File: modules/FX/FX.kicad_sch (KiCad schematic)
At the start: 0 parts

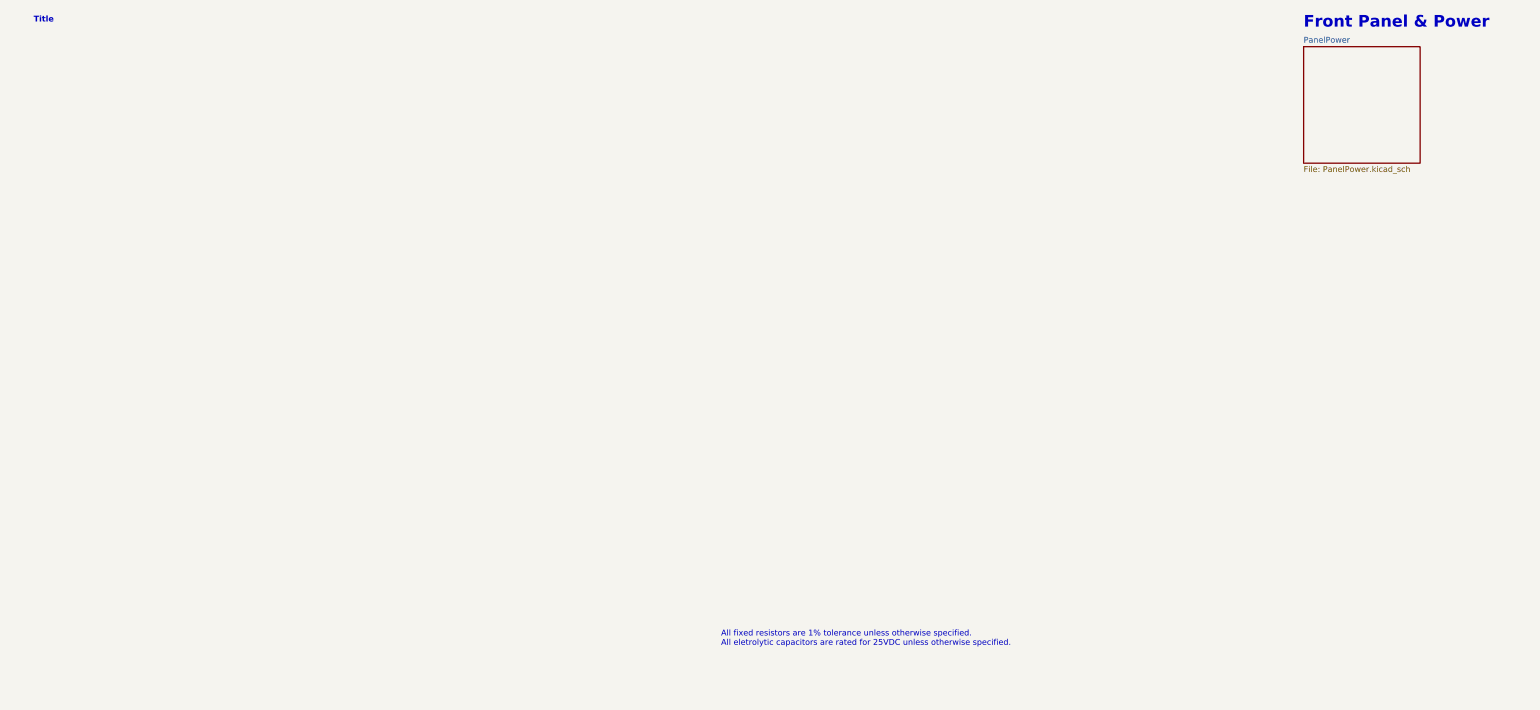
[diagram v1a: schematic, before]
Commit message: FX module - preliminary schematic done
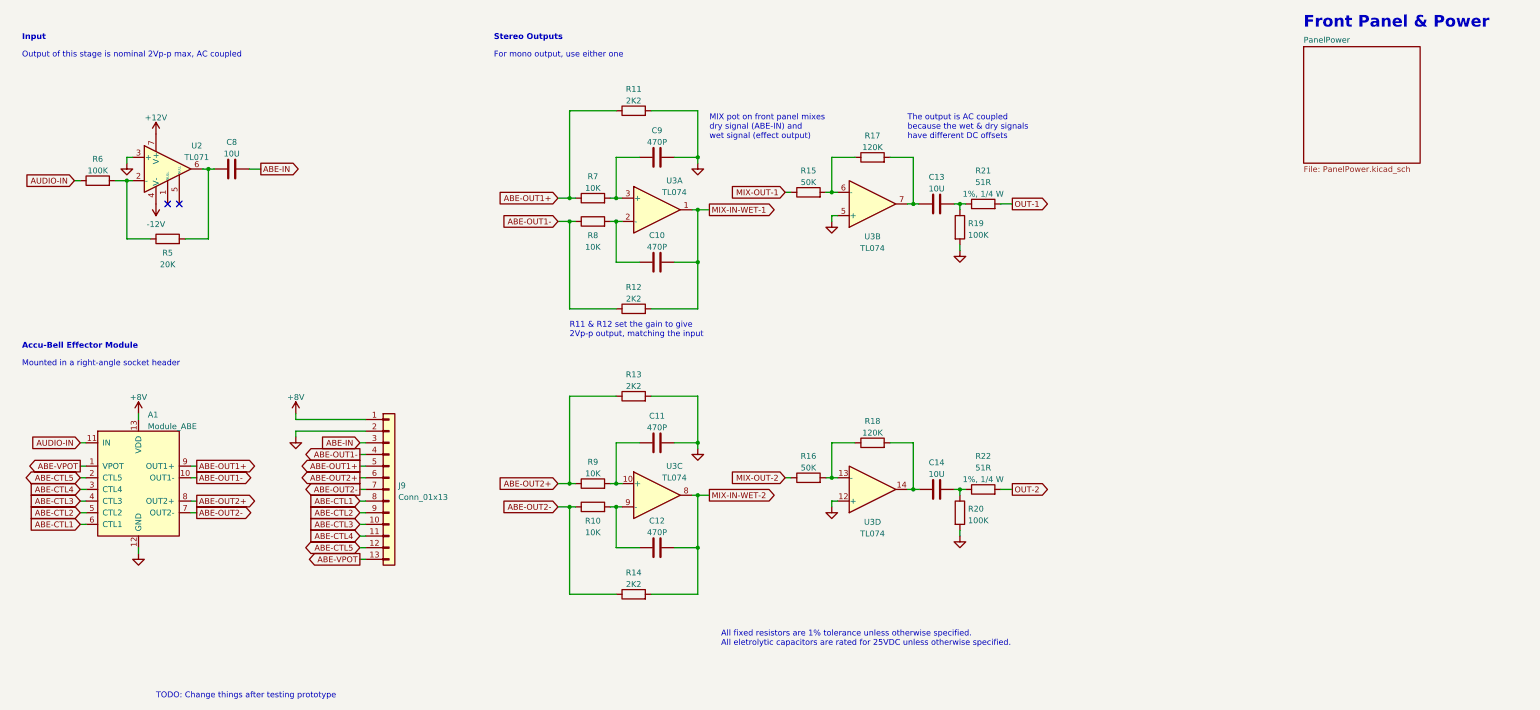
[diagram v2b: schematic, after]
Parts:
- added A1: Module_ABE, -lmp-synth:Module_ABE_Vert, symbol -lmp-synth:Module_ABE
- added C10, C11, C12, C9: 470P, symbol -lmp:CC
- added C13, C14, C8: 10U, -lmp-misc:C_Radial_D5.0mm_H5.0mm_P2.50mm, symbol -lmp-synth:CNP_10U
- added J9: Conn_01x13, Connector_PinSocket_2.54mm:PinSocket_1x13_P2.54mm_Horizontal, symbol Connector_Generic:Conn_01x13
- added R10, R7, R8, R9: 10K, -lmp-misc:R_Axial_DIN0207_L6.3mm_D2.5mm_P7.62mm_Horizontal, symbol -lmp:R_1%_0W166
- added R11, R12, R13, R14: 2K2, -lmp-misc:R_Axial_DIN0207_L6.3mm_D2.5mm_P7.62mm_Horizontal, symbol -lmp:R_1%_0W166
- added R15, R16: 50K, -lmp-misc:R_Axial_DIN0207_L6.3mm_D2.5mm_P7.62mm_Horizontal, symbol -lmp:R_1%_0W166
- added R17, R18: 120K, -lmp-misc:R_Axial_DIN0207_L6.3mm_D2.5mm_P7.62mm_Horizontal, symbol -lmp:R_1%_0W166
- added R19, R20, R6: 100K, -lmp-misc:R_Axial_DIN0207_L6.3mm_D2.5mm_P7.62mm_Horizontal, symbol -lmp:R_1%_0W166
- added R21, R22: 51R, -lmp-misc:R_Axial_DIN0207_L6.3mm_D2.5mm_P10.16mm_Horizontal, symbol -lmp-synth:R_51R_Output
- added R5: 20K, -lmp-misc:R_Axial_DIN0207_L6.3mm_D2.5mm_P7.62mm_Horizontal, symbol -lmp:R_1%_0W166
- added U2: TL071, Package_DIP:DIP-8_W7.62mm, symbol -lmp-opamp:TL071
- added U3: TL074, Package_DIP:DIP-14_W7.62mm, symbol -lmp-opamp:TL074
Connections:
- new net: C9.1, R7.2, U3.3 (+)
- new net: C10.1, R8.2, U3.2 (-)
- new net: R5.1, R6.2, U2.2 (-)
- new net: R16.2, R18.1, U3.13 (-)
- new net: C14.1, R18.2, U3.14
- new net: C14.2, R20.1, R22.1
- new net: R15.2, R17.1, U3.6 (-)
- new net: C13.1, R17.2, U3.7
- new net: C13.2, R19.1, R21.1
- new net: C8.1, R5.2, U2.6
- new net: C11.1, R9.2, U3.10 (+)
- new net: C12.1, R10.2, U3.9 (-)
- new net +12V: U2.7 (V+)
- new net +8V: A1.13 (VDD), J9.1 (Pin_1)
- new net -12V: U2.4 (V-)
- new net ABE-CTL1: A1.6 (CTL1), J9.8 (Pin_8)
- new net ABE-CTL2: A1.5 (CTL2), J9.9 (Pin_9)
- new net ABE-CTL3: A1.4 (CTL3), J9.10 (Pin_10)
- new net ABE-CTL4: A1.3 (CTL4), J9.11 (Pin_11)
- new net ABE-CTL5: A1.2 (CTL5), J9.12 (Pin_12)
- new net ABE-IN: C8.2, J9.3 (Pin_3)
- new net ABE-OUT1+: A1.9 (OUT1+), J9.5 (Pin_5), R11.1, R7.1
- new net ABE-OUT1-: A1.10 (OUT1-), J9.4 (Pin_4), R12.1, R8.1
- new net ABE-OUT2+: A1.8 (OUT2+), J9.6 (Pin_6), R13.1, R9.1
- new net ABE-OUT2-: A1.7 (OUT2-), J9.7 (Pin_7), R10.1, R14.1
- new net ABE-VPOT: A1.1 (VPOT), J9.13 (Pin_13)
- new net AUDIO-IN: A1.11 (IN), R6.1
- new net GND: A1.12 (GND), C11.2, C9.2, J9.2 (Pin_2), R11.2, R13.2, R19.2, R20.2, U2.3 (+), U3.12 (+), U3.5 (+)
- new net MIX-IN-WET-1: C10.2, R12.2, U3.1
- new net MIX-IN-WET-2: C12.2, R14.2, U3.8
- new net MIX-OUT-1: R15.1
- new net MIX-OUT-2: R16.1
- new net OUT-1: R21.2
- new net OUT-2: R22.2
- no-connect marks 0 -> 2
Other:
- note added: "Accu-Bell Effector Module"
- note added: "For mono output, use either one"
- note added: "Input"
- note added: "MIX pot on front panel mixes dry signal (ABE-IN) and wet signal (effect output)"
- note added: "Mounted in a right-angle socket header"
- note added: "Output of this stage is nominal 2Vp-p max, AC coupled"
- note added: "R11 & R12 set the gain to give 2Vp-p output, matching the input"
- note added: "Stereo Outputs"
- note added: "TODO: Change things after testing prototype"
- note added: "The output is AC coupled because the wet & dry signals have different DC offsets"
- note removed: "Title"

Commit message: FX module - update schematic based on prototype
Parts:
- A1: footprint -lmp-synth:Module_ABE_Vert -> -lmp-synth:Module_ABE_Horiz_NoPads
- R21, R22: value 51R -> 270R; DistributorPartLink https://www.mouser.ca/ProductDetail/?qs=oAGoVhmvjhzVx2bdEH1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 -> https://www.mouser.ca/ProductDetail/YAGEO/MFR-25FRF52-270R?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; DistributorPartNum 603-MFR-25FBF52-51R -> 603-MFR-25FRF52-270R; ManufacturerPartNum MFR-25FBF52-51R -> MFR-25FRF52-270R
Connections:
- net +8V: now also J9.13 (Pin_13); no longer J9.1 (Pin_1)
- net ABE-CTL1: now also J9.6 (Pin_6); no longer J9.8 (Pin_8)
- net ABE-CTL2: now also J9.5 (Pin_5); no longer J9.9 (Pin_9)
- net ABE-CTL3: now also J9.4 (Pin_4); no longer J9.10 (Pin_10)
- net ABE-CTL4: now also J9.3 (Pin_3); no longer J9.11 (Pin_11)
- net ABE-CTL5: now also J9.2 (Pin_2); no longer J9.12 (Pin_12)
- net ABE-IN: now also J9.11 (Pin_11); no longer J9.3 (Pin_3)
- net ABE-OUT1+: now also J9.9 (Pin_9); no longer J9.5 (Pin_5)
- net ABE-OUT1-: now also J9.10 (Pin_10); no longer J9.4 (Pin_4)
- net ABE-OUT2+: now also J9.8 (Pin_8); no longer J9.6 (Pin_6)
- net ABE-VPOT: now also J9.1 (Pin_1); no longer J9.13 (Pin_13)
- net GND: now also J9.12 (Pin_12); no longer J9.2 (Pin_2)
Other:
- note added: "Convert differential signals to Eurorack audio level outputs. For mono output, use either one."
- note added: "TODO: Verify output level"
- note added: "The MIX pot on the front panel mixes the dry signal (ABE-IN) and wet signal (effect output)"
- note removed: "For mono output, use either one"
- note removed: "MIX pot on front panel mixes dry signal (ABE-IN) and wet signal (effect output)"
- note removed: "TODO: Change things after testing prototype"
- moved on the sheet: C13, C14, R15, R16, R17, R18, R19, R20, R21, U3B, U3D

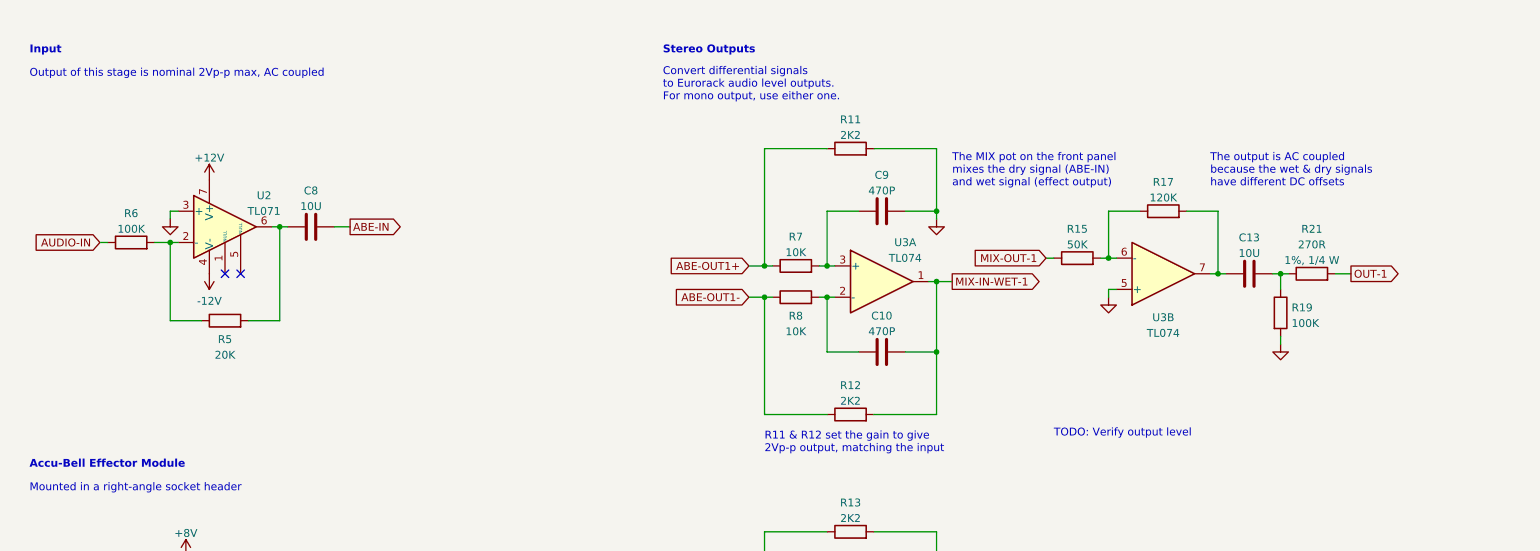
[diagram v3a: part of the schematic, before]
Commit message: FX module - update schematic after testing
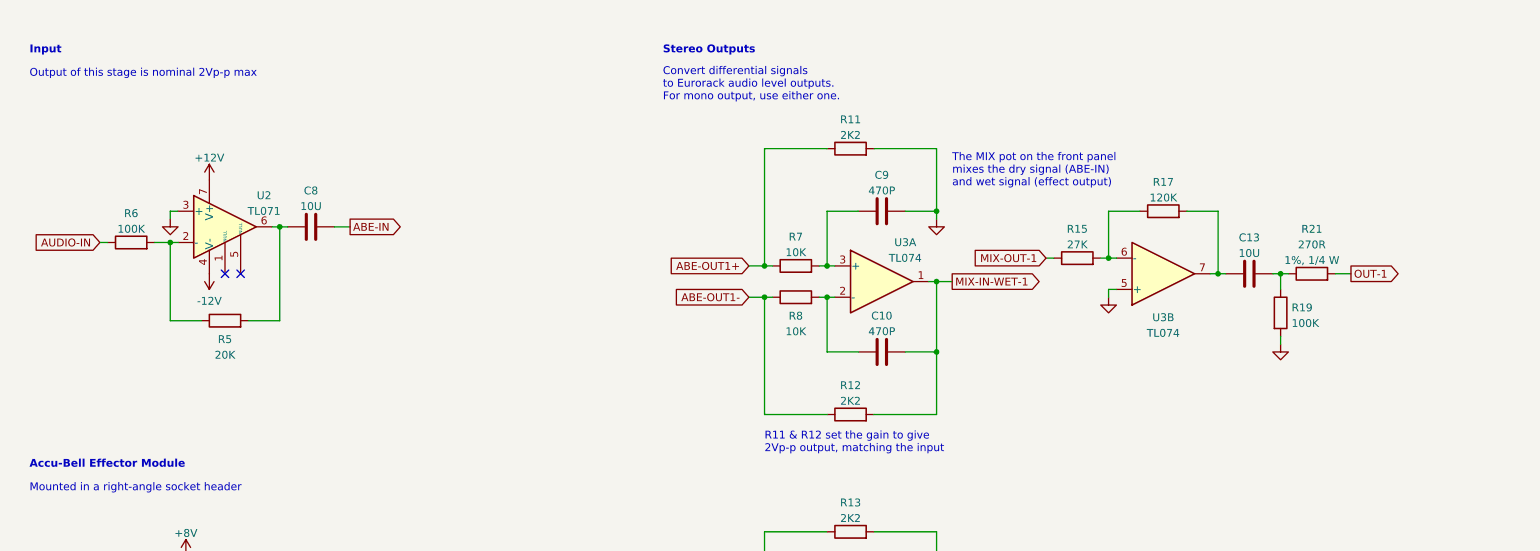
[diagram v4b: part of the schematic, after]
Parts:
- R15: value 50K -> 27K
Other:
- note added: "Output of this stage is nominal 2Vp-p max"
- note removed: "Output of this stage is nominal 2Vp-p max, AC coupled"
- note removed: "TODO: Verify output level"
- note removed: "The output is AC coupled because the wet & dry signals have different DC offsets"
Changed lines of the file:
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@@
-    (effects (font (size 1.27 1.27)) (justify left bottom))
-  )
-  (text "TODO: Verify output level" (at 191.77 86.36 0)
     (effects (font (size 1.27 1.27)) (justify left bottom))
   )
@@
     (effects (font (size 1.27 1.27) bold) (justify left bottom))
   )
-  (text "The output is AC coupled \nbecause the wet & dry signals \nhave different DC offsets"
-    (at 217.17 45.72 0)
-    (effects (font (size 1.27 1.27)) (justify left bottom))
-  )
   (text "Input" (at 25.4 24.13 0)
     (effects (font (size 1.27 1.27) (thickness 0.254) bold) (justify left bottom))
@@
     (effects (font (size 2.54 2.54) (thickness 0.508) bold) (justify left bottom))
   )
-  (text "Output of this stage is nominal 2Vp-p max, AC coupled"
-    (at 25.4 27.94 0)
+  (text "Output of this stage is nominal 2Vp-p max" (at 25.4 27.94 0)
     (effects (font (size 1.27 1.27)) (justify left bottom))
   )
@@
     (in_bom yes) (on_board yes) (fields_autoplaced)
     (property "Reference" "R15" (id 0) (at 195.58 52.4342 90))
-    (property "Value" "50K" (id 1) (at 195.58 54.9711 90))
+    (property "Value" "27K" (id 1) (at 195.58 54.9711 90))
     (property "Footprint" "-lmp-misc:R_Axial_DIN0207_L6.3mm_D2.5mm_P7.62mm_Horizontal" (id 2) (at 195.58 58.928 90)
       (effects (font (size 1.27 1.27)) hide)
@@
     )
     (path "/ea745f03-d3ce-4a1a-9ef3-c9f64a4f1bbe"
-      (reference "R15") (unit 1) (value "50K") (footprint "-lmp-misc:R_Axial_DIN0207_L6.3mm_D2.5mm_P7.62mm_Horizontal")
+      (reference "R15") (unit 1) (value "27K") (footprint "-lmp-misc:R_Axial_DIN0207_L6.3mm_D2.5mm_P7.62mm_Horizontal")
     )
     (path "/f0688393-00a6-44d1-a67d-6b45d3a18d2e"

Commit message: FX module - wip
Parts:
- removed U2: TL071, Package_DIP:DIP-8_W7.62mm, symbol -lmp-opamp:TL071
- added C14, C15: 10P, -lmp-misc:C_Disc_D5.0mm_W2.5mm_P2.50mm, symbol -lmp:CF
- added C9: 10U, -lmp-misc:C_Radial_D5.0mm_H5.0mm_P2.50mm, symbol -lmp-synth:CNP_10U
- added U2: TL072, Package_DIP:DIP-8_W7.62mm, symbol -lmp-opamp:TL072
- C10: renamed from C9; footprint (none) -> -lmp-misc:C_Disc_D5.0mm_W2.5mm_P2.50mm; Distributor (none) -> Mouser; DistributorPartLink (none) -> https://www.mouser.ca/ProductDetail/TDK/FA18C0G1H471JNU00?q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; DistributorPartNum (none) -> 810-FA18C0G1H47100; Manufacturer (none) -> TDK; ManufacturerPartNum (none) -> FA18C0G1H471JNU00; Value2 (none) -> C0G/NP0
- C11: renamed from C10; footprint (none) -> -lmp-misc:C_Disc_D5.0mm_W2.5mm_P2.50mm; Distributor (none) -> Mouser; DistributorPartLink (none) -> https://www.mouser.ca/ProductDetail/TDK/FA18C0G1H471JNU00?q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; DistributorPartNum (none) -> 810-FA18C0G1H47100; Manufacturer (none) -> TDK; ManufacturerPartNum (none) -> FA18C0G1H471JNU00; Value2 (none) -> C0G/NP0
- C12: renamed from C11; footprint (none) -> -lmp-misc:C_Disc_D5.0mm_W2.5mm_P2.50mm; Distributor (none) -> Mouser; DistributorPartLink (none) -> https://www.mouser.ca/ProductDetail/TDK/FA18C0G1H471JNU00?q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; DistributorPartNum (none) -> 810-FA18C0G1H47100; Manufacturer (none) -> TDK; ManufacturerPartNum (none) -> FA18C0G1H471JNU00; Value2 (none) -> C0G/NP0
- C13: renamed from C12; footprint (none) -> -lmp-misc:C_Disc_D5.0mm_W2.5mm_P2.50mm; Distributor (none) -> Mouser; DistributorPartLink (none) -> https://www.mouser.ca/ProductDetail/TDK/FA18C0G1H471JNU00?q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; DistributorPartNum (none) -> 810-FA18C0G1H47100; Manufacturer (none) -> TDK; ManufacturerPartNum (none) -> FA18C0G1H471JNU00; Value2 (none) -> C0G/NP0
- R15: value 27K -> 20K
- R16: value 50K -> 20K
- R17, R18: value 120K -> 100K
- renumbered C13 to C16, C14 to C17
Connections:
- net GND: now also U2.3 (+)
- net at R5.1, R6.2: now also U2.2 (-)
- net at R16.2, R18.1, U3.13 (-): now also C15.1
- net at C17.1, R18.2, U3.14: now also C15.2
- net at R15.2, R17.1, U3.6 (-): now also C14.1
- net at C16.1, R17.2, U3.7: now also C14.2
- net at C8.1, R5.2: now also U2.1, U2.5 (+)
- new net: C9.1, U2.6 (-), U2.7
- new net MIX-IN-DRY: C9.2
- no-connect marks 2 -> 0
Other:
- note added: "Separately buffered signals for the fx module and the mixer"
- note added: "TODO: can use polarized caps?"
- note added: "The MIX pot on the front panel mixes the dry (input) signal with the wet signal (effect output)"
- note removed: "The MIX pot on the front panel mixes the dry signal (ABE-IN) and wet signal (effect output)"
- moved on the sheet: C8, J9, R5, R6

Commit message: FX module - pcb layout wip
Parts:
- A1: ManufacturerPartNum ABE -> ABE-01
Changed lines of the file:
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@@
       (effects (font (size 1.27 1.27)) hide)
     )
-    (property "ManufacturerPartNum" "ABE" (id 5) (at 50.8 120.65 0)
+    (property "ManufacturerPartNum" "ABE-01" (id 5) (at 50.8 120.65 0)
       (effects (font (size 1.27 1.27)) hide)
     )

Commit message: FX module - pcb layout wip
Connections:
- net GND: now also U2.5 (+); no longer U2.3 (+)
- net at R5.1, R6.2: now also U2.6 (-); no longer U2.2 (-)
- net at C8.1, R5.2: now also U2.3 (+), U2.7; no longer U2.1, U2.5 (+)
- new net: C9.1, U2.1, U2.2 (-)
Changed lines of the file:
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@@
     (pin "2")
   )
-  (symbol (lib_id "-lmp-opamp:TL072") (at 76.2 63.5 0) (unit 2)
+  (symbol (lib_id "-lmp-opamp:TL072") (at 76.2 63.5 0) (unit 1)
     (in_bom yes) (on_board yes) (fields_autoplaced)
     (property "Reference" "U2" (id 0) (at 76.2 54.7202 0))
@@
     (pin "8")
   )
-  (symbol (lib_id "-lmp-opamp:TL072") (at 57.15 48.26 0) (mirror x) (unit 1)
+  (symbol (lib_id "-lmp-opamp:TL072") (at 57.15 48.26 0) (mirror x) (unit 2)
     (in_bom yes) (on_board yes) (fields_autoplaced)
     (property "Reference" "U2" (id 0) (at 57.15 55.3704 0))
@@
       (reference "U1") (unit 1) (value "LM7808_TO220") (footprint "Package_TO_SOT_THT:TO-220-3_Vertical")
     )
+    (path "/da1e36fb-0c95-45a4-b7c5-887fd123a916"
+      (reference "U2") (unit 1) (value "TL072") (footprint "Package_DIP:DIP-8_W7.62mm")
+    )
     (path "/ddea2031-0391-496d-9117-3226824f2e27"
-      (reference "U2") (unit 1) (value "TL072") (footprint "Package_DIP:DIP-8_W7.62mm")
-    )
-    (path "/da1e36fb-0c95-45a4-b7c5-887fd123a916"
       (reference "U2") (unit 2) (value "TL072") (footprint "Package_DIP:DIP-8_W7.62mm")
     )
